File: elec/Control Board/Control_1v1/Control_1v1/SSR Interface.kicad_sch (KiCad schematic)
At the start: 6 parts, among them Q601 BSS138

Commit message: Add sheet with title block.
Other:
- company: (none) -> Public Invention
- title: (none) -> Control Interconnect Board

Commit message: Fix J10 backwards.
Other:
- title: Control Interconnect Board -> Control Interconnect Board OEDCS
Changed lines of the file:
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@@
   (paper "USLedger")
   (title_block
-    (title "Control Interconnect Board")
+    (title "Control Interconnect Board OEDCS")
     (date "2023-10-10")
     (rev "Rev 1.1")
     (company "Public Invention")
-    (comment 1 "Contributor: Lawrence Kinceloe")
+    (comment 1 "GNU Affero General Public License v3.0")
+    (comment 2 "Contributor: Lawrence Kinceloe")
+    (comment 3 "Drawn By: (Forrest) Lee Erickson")
   )
   (junction (at 101.6 41.91) (diameter 0) (color 0 0 0 0)

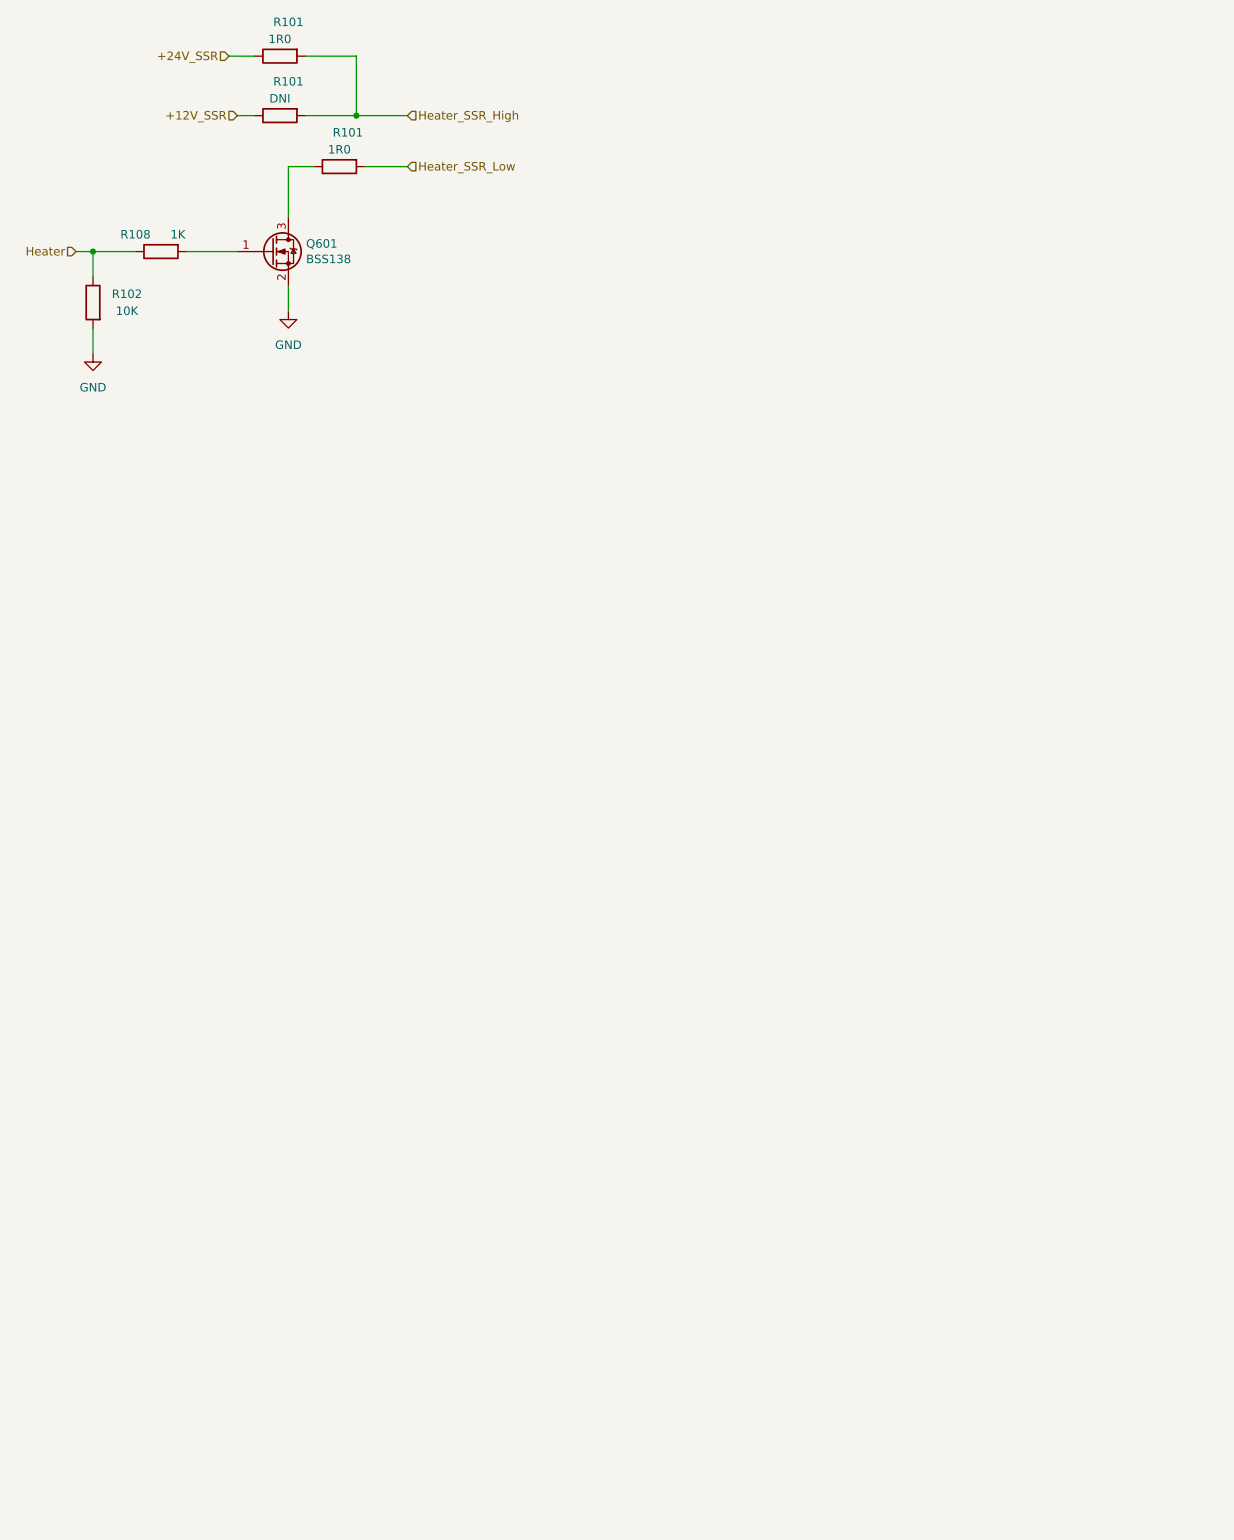
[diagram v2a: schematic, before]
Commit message: Add second power supply connector. Add second and third SSR Driver. Add reset discharge.
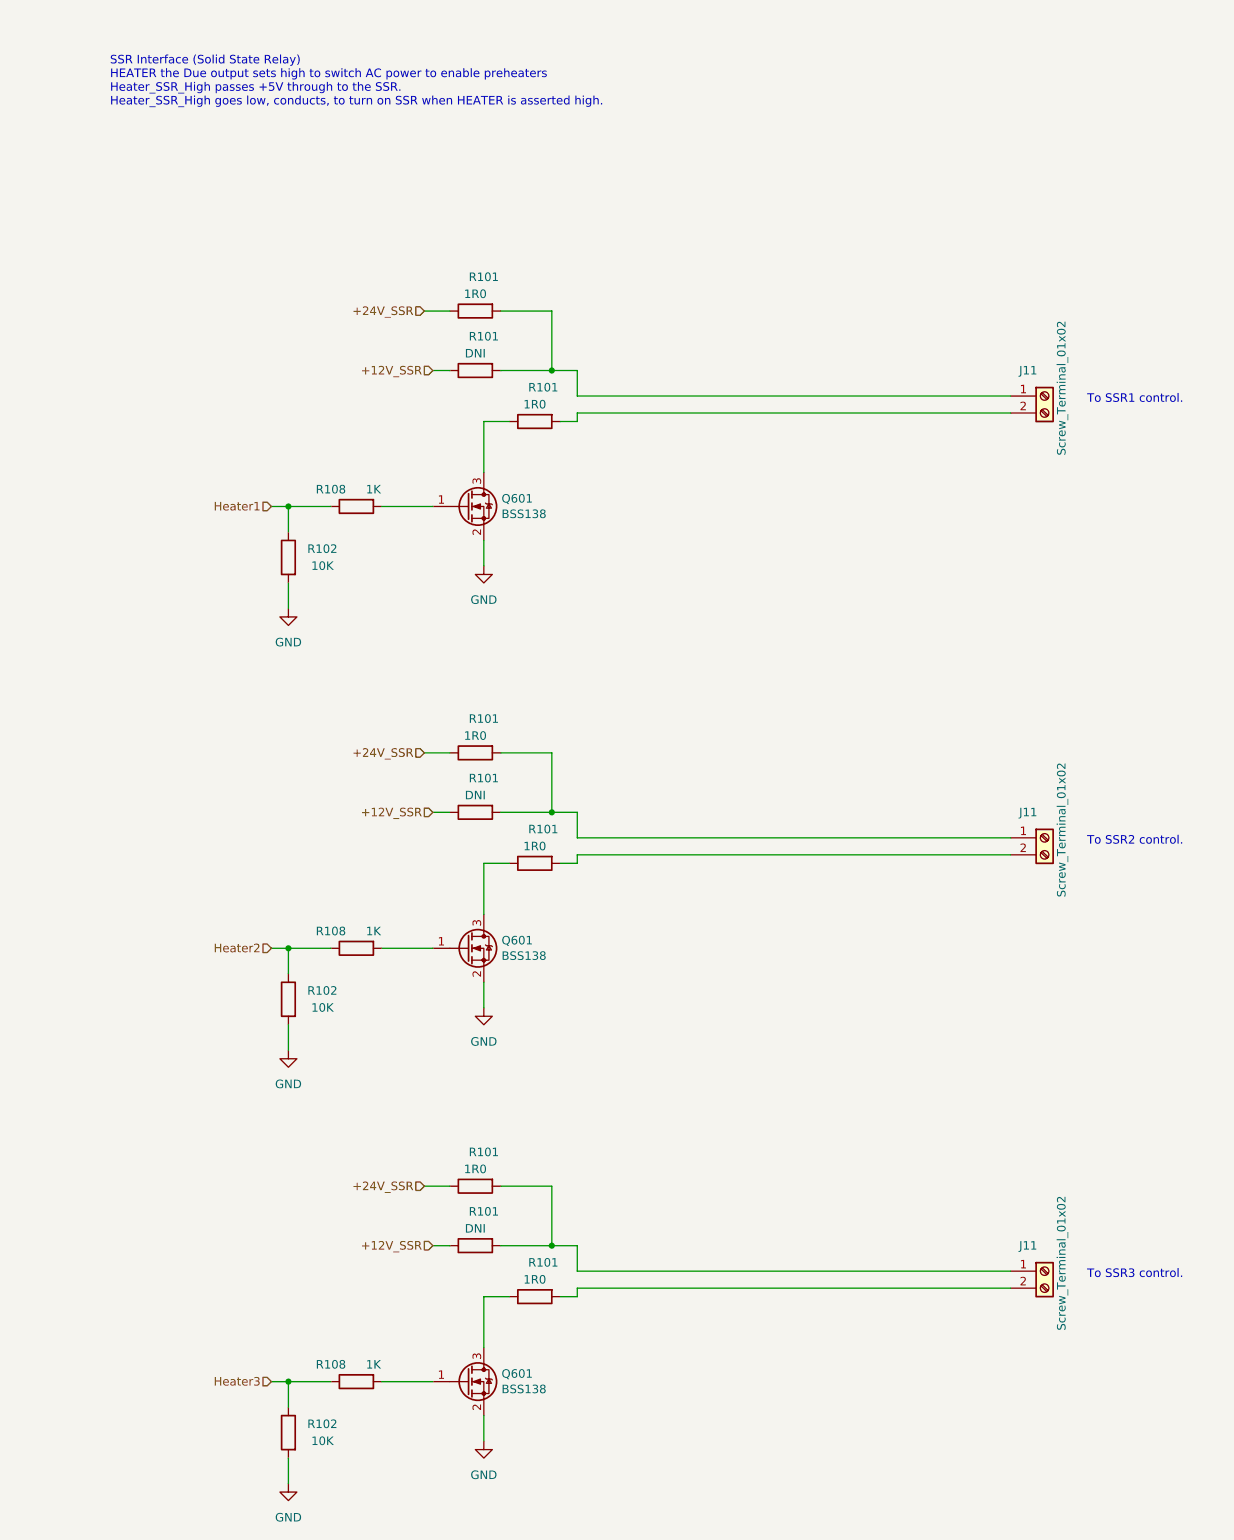
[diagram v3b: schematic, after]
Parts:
- added J11 (x3): Screw_Terminal_01x02, TerminalBlock_TE-Connectivity:TerminalBlock_TE_282834-2_1x02_P2.54mm_Horizontal, symbol Connector:Screw_Terminal_01x02
- added Q601 (x2): BSS138, Package_TO_SOT_SMD:SOT-23, symbol Transistor_FET:BSS138
- added R101 (x4): 1R0, Resistor_SMD:R_0603_1608Metric_Pad0.98x0.95mm_HandSolder, symbol Device:R
- added R101 (x2): DNI, Resistor_SMD:R_0603_1608Metric_Pad0.98x0.95mm_HandSolder, symbol Device:R
- added R102 (x2): 10K, Resistor_SMD:R_0603_1608Metric_Pad0.98x0.95mm_HandSolder, symbol Device:R
- added R108 (x2): 1K, Resistor_SMD:R_0603_1608Metric_Pad0.98x0.95mm_HandSolder, symbol Device:R
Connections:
- net +12V_SSR: now also R101.1, R101.1
- net +24V_SSR: now also R101.1, R101.1
- net GND: now also Q601.2 (S), Q601.2 (S), R102.2, R102.2
- net Heater renamed Heater1
- net Heater_SSR_High: no longer names the net of R101.2, R101.2
- net Heater_SSR_High: now also J11.1 (Pin_1)
- net Heater_SSR_Low: no longer names the net of R101.2
- net Heater_SSR_Low: now also J11.2 (Pin_2)
- new net: Q601.1 (G), R108.2 (x2)
- new net: Q601.3 (D), R101.1 (x2)
- new net: J11.2 (Pin_2), R101.2 (x2)
- new net: J11.1 (Pin_1), R101.2, R101.2 (x2)
- new net Heater2: R102.1, R108.1
- new net Heater3: R102.1, R108.1
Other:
- note added: "SSR Interface (Solid State Relay) HEATER the Due output sets high to switch AC power to enable preheaters Heater_SSR_High passes +5V through to the SSR. Heater_SSR_High goes low, conducts, to turn on SSR when HEATER is asserted high."
- note added: "To SSR1 control."
- note added: "To SSR2 control."
- note added: "To SSR3 control."
- moved on the sheet: Q601, R101, R102, R108

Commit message: Add power shutdown button. Add thermocouple ground screw terminals. Isolate SCL from SDA traces. Make first cut BOM.
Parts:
- R101: LongLead (none) -> NO
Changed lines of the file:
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@@
+      (effects (font (size 1.27 1.27)) hide)
+    )
+    (property "LongLead" "NO" (at 128.27 87.63 0)
       (effects (font (size 1.27 1.27)) hide)
     )
@@
     )
     (property "Cost" "0.0015" (at 128.27 153.67 0)
+      (effects (font (size 1.27 1.27)) hide)
+    )
+    (property "LongLead" "NO" (at 128.27 153.67 0)
       (effects (font (size 1.27 1.27)) hide)
     )
@@
       (effects (font (size 1.27 1.27)) hide)
     )
+    (property "LongLead" "NO" (at 119.38 201.93 0)
+      (effects (font (size 1.27 1.27)) hide)
+    )
     (pin "1")
     (pin "2")
@@
       (effects (font (size 1.27 1.27)) hide)
     )
+    (property "LongLead" "NO" (at 119.38 71.12 0)
+      (effects (font (size 1.27 1.27)) hide)
+    )
     (pin "1")
     (pin "2")
@@
     )
     (property "Cost" "0.0015" (at 119.38 137.16 0)
+      (effects (font (size 1.27 1.27)) hide)
+    )
+    (property "LongLead" "NO" (at 119.38 137.16 0)
       (effects (font (size 1.27 1.27)) hide)
     )
@@
       (effects (font (size 1.27 1.27)) hide)
     )
+    (property "LongLead" "NO" (at 128.27 218.44 0)
+      (effects (font (size 1.27 1.27)) hide)
+    )
